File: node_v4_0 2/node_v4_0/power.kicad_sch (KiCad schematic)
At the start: 24 parts, among them J1 Conn_01x02_Pin, J2 12402012E212A, Q1 DMG2301L, U13 MAX31342EWA+T, U3 AP2112K-3.3, U4 CAT3200-5, U5 MCP73831-2-OT

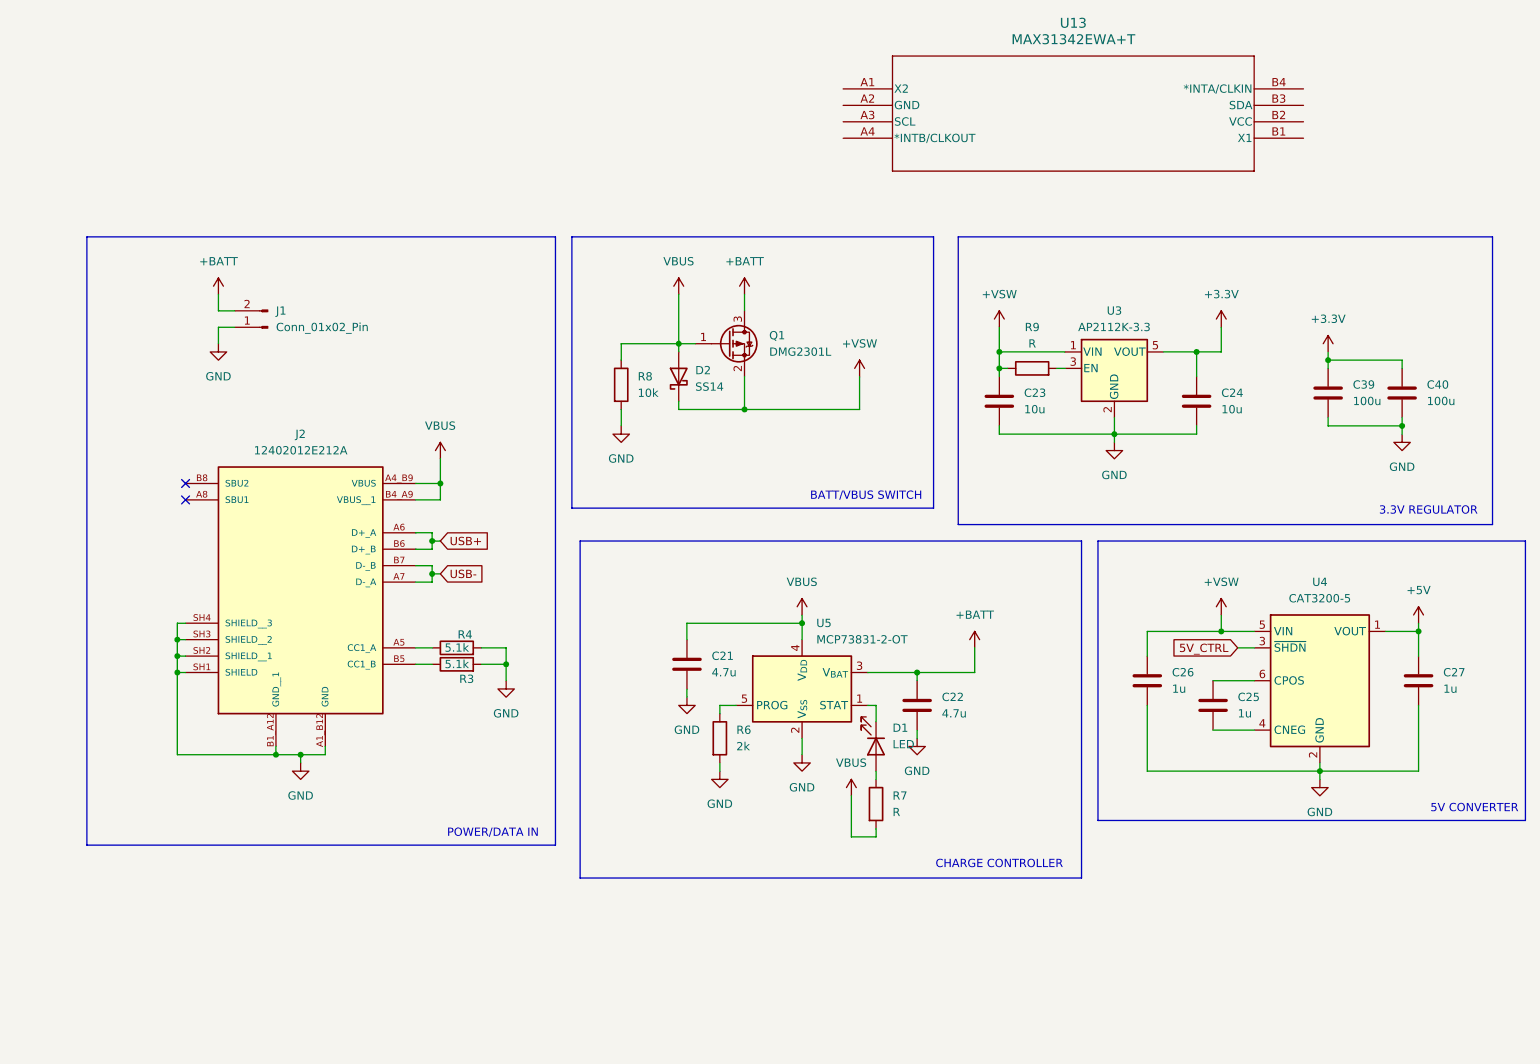
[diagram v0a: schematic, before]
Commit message: finished laying out the board
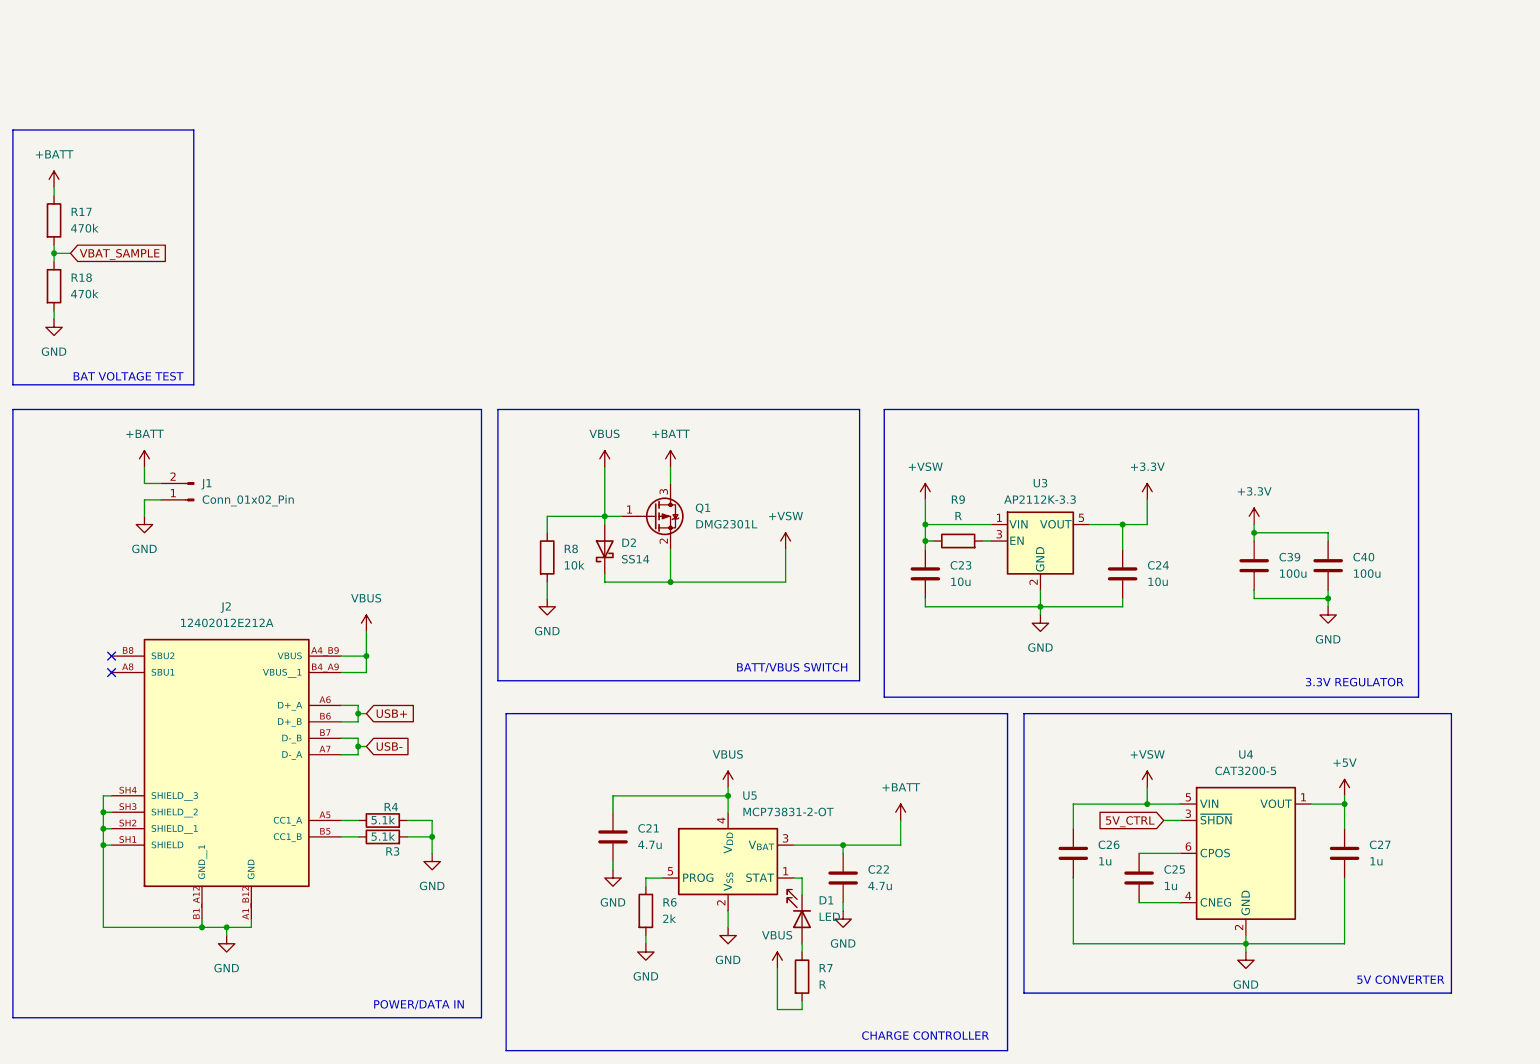
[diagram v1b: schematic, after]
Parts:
- removed U13: MAX31342EWA+T, WiSDOM:21-100291_W80D&plus_1_MXM, symbol WiSDOM:MAX31342EWA+T
- added R17, R18: 470k, Resistor_SMD:R_0805_2012Metric_Pad1.20x1.40mm_HandSolder, symbol Device:R
- J2: footprint usbc:AMPHENOL_12402012E212A -> WiSDOM:AMPHENOL_12402012E212A
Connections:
- net +BATT: now also R17.1
- net GND: now also R18.2
- new net VBAT_SAMPLE: R17.2, R18.1
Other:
- note added: "BAT VOLTAGE TEST"
- moved on the sheet: C21, C22, C23, C24, C25, C26, C27, C39, C40, D1, D2, J1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

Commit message: most routing done
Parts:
- added BT1: RTC_BAT, WiSDOM:BAT_BAT-HLD-001-THM, symbol Device:Battery_Cell
- added C46: 10u, Capacitor_SMD:C_0805_2012Metric_Pad1.18x1.45mm_HandSolder, symbol Device:C
- added D3: SS14, Diode_SMD:D_SMA, symbol Diode:SS14
- added Q2: DMG2301L, Package_TO_SOT_SMD:SOT-23, symbol Transistor_FET:DMG2301L
- added R19: 100k, Resistor_SMD:R_0805_2012Metric_Pad1.20x1.40mm_HandSolder, symbol Device:R
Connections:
- net +3.3V: now also D3.2 (A), Q2.1 (G), R19.1
- net GND: now also BT1.2 (-), C46.2, R19.2
- new net +VRTC: C46.1, D3.1 (K), Q2.2 (S)
- new net RTC_BAT: BT1.1 (+), Q2.3 (D)

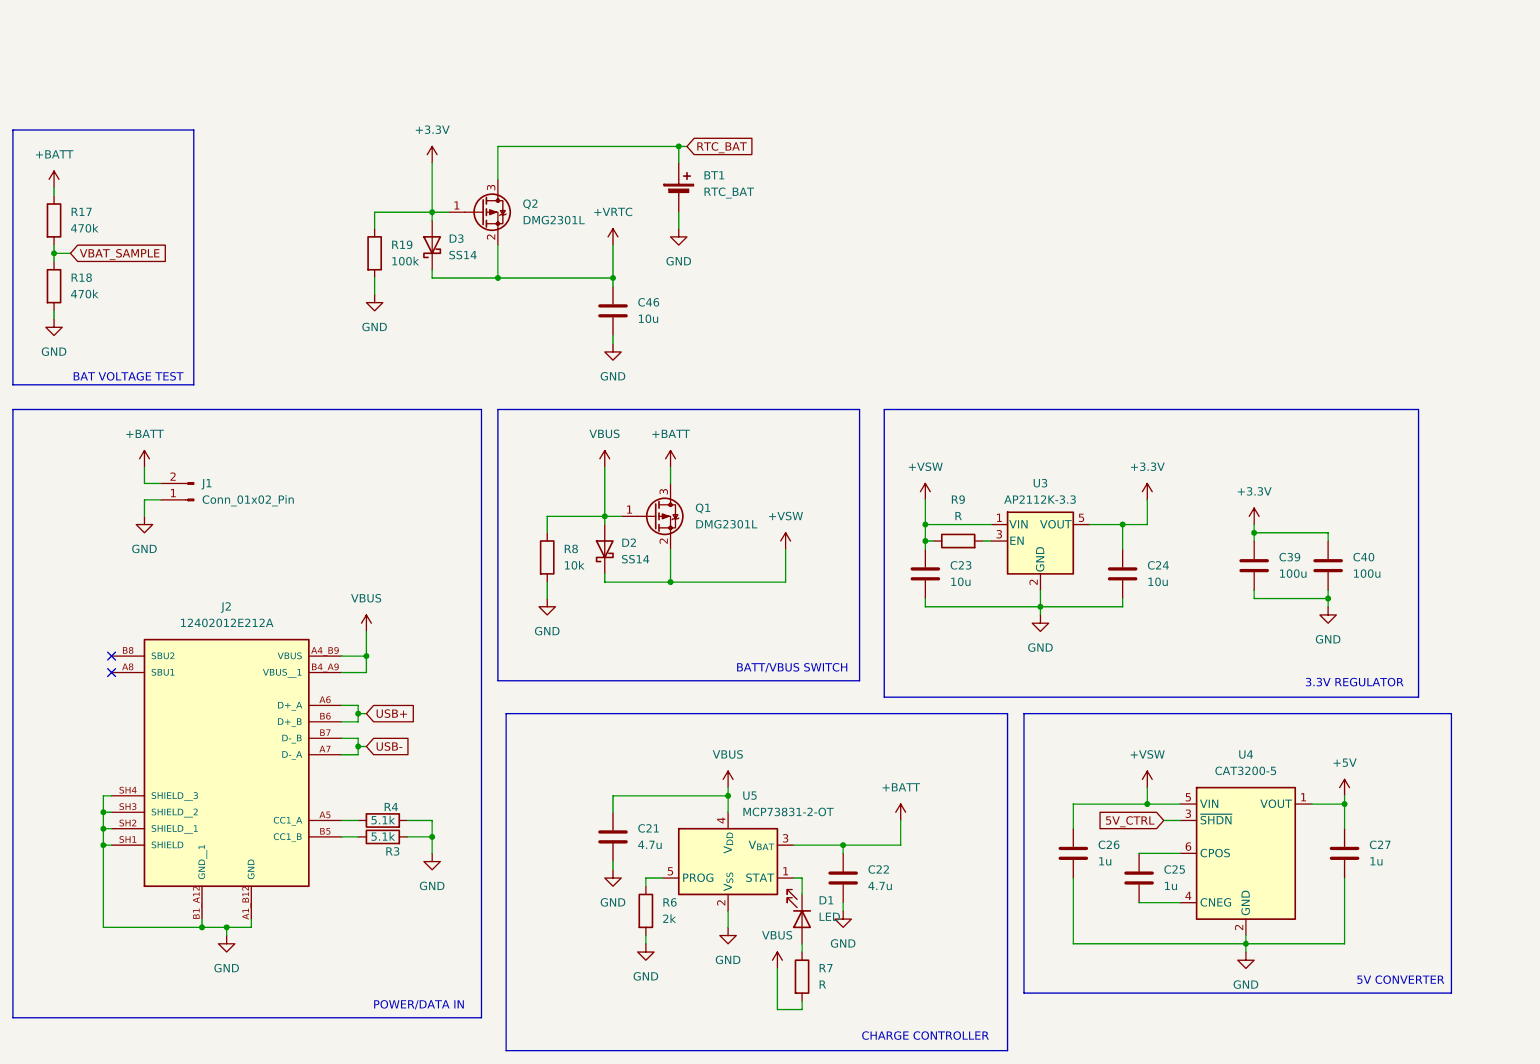
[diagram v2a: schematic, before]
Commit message: moved reset button to make space for vin jst connector
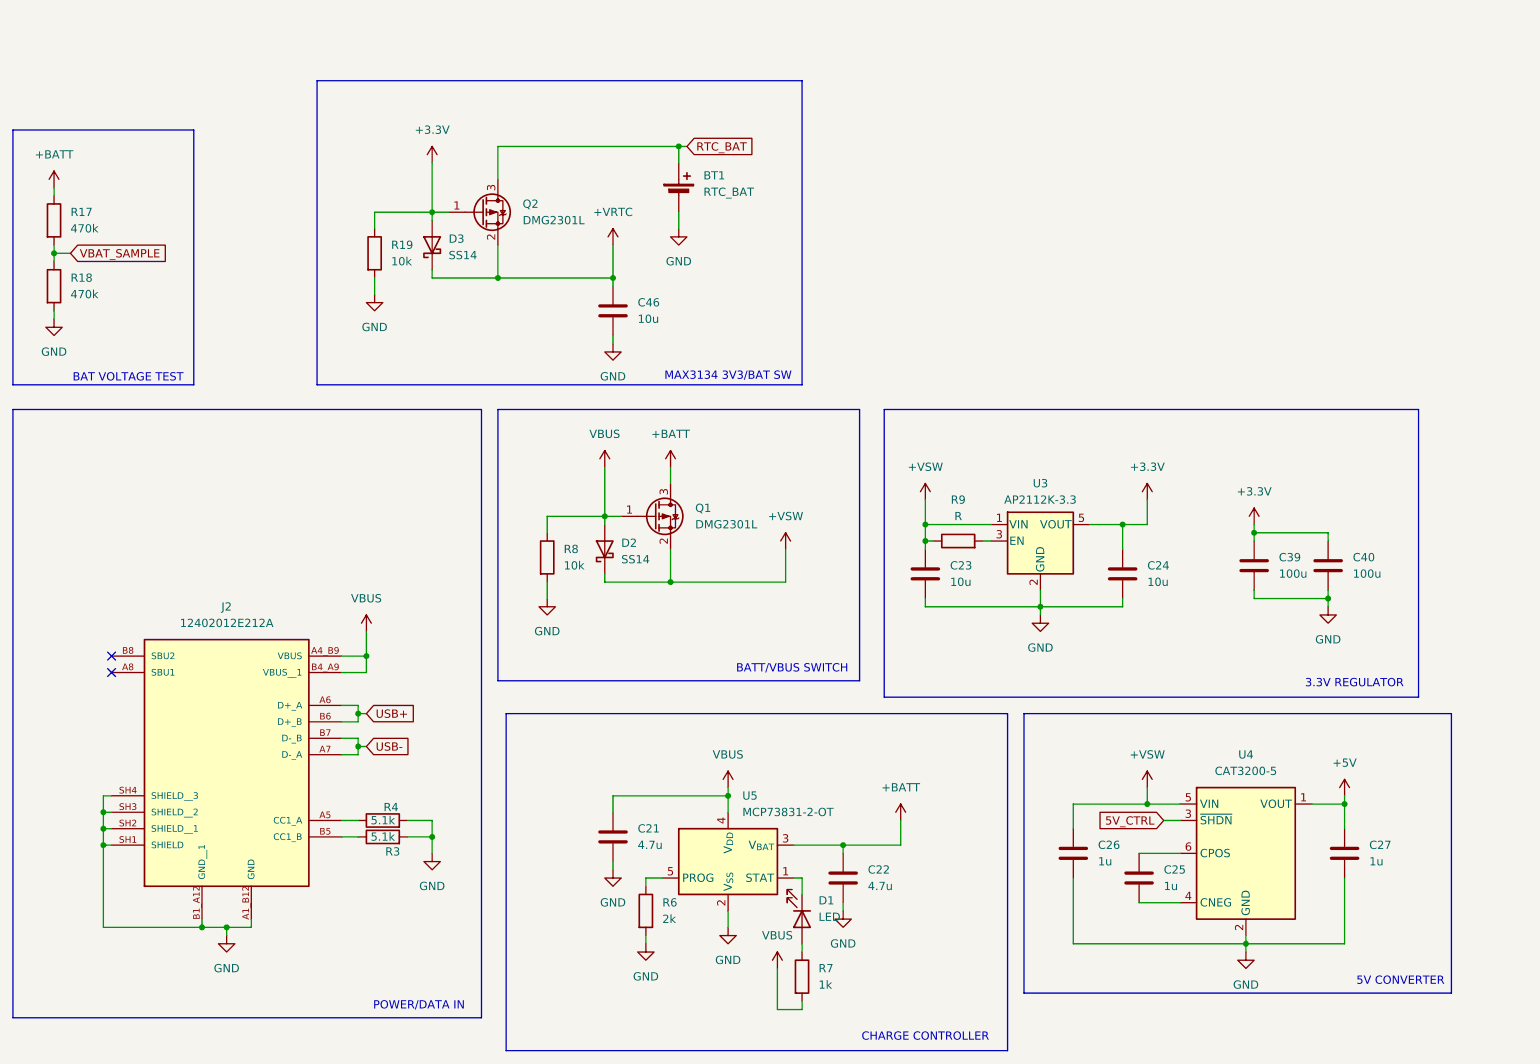
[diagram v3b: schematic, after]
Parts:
- removed J1: Conn_01x02_Pin, Connector_JST:JST_PH_S2B-PH-K_1x02_P2.00mm_Horizontal, symbol Connector:Conn_01x02_Pin
- R19: value 100k -> 10k
- R7: value R -> 1k
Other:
- note added: "MAX3134 3V3/BAT SW"
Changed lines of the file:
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@@
 	(wire
 		(pts
-			(xy 41.91 82.55) (xy 41.91 85.09)
-		)
-		(stroke
-			(width 0)
-			(type default)
-		)
-	)
-	(wire
-		(pts
 			(xy 143.51 166.37) (xy 143.51 165.1)
 		)
@@
 	(wire
 		(pts
-			(xy 41.91 85.09) (xy 44.45 85.09)
-		)
-		(stroke
-			(width 0)
-			(type default)
-		)
-	)
-	(wire
-		(pts
 			(xy 74.93 124.46) (xy 74.93 125.73)
 		)
@@
 	(wire
 		(pts
-			(xy 41.91 87.63) (xy 44.45 87.63)
-		)
-		(stroke
-			(width 0)
-			(type default)
-		)
-	)
-	(wire
-		(pts
 			(xy 124.46 33.02) (xy 96.52 33.02)
 		)
@@
 	(wire
 		(pts
-			(xy 41.91 90.17) (xy 41.91 87.63)
-		)
-		(stroke
-			(width 0)
-			(type default)
-		)
-	)
-	(wire
-		(pts
 			(xy 86.36 43.18) (xy 88.9 43.18)
 		)
@@
 	)
 	(rectangle
+		(start 68.58 22.86)
+		(end 143.51 69.85)
+		(stroke
+			(width 0)
+			(type default)
+		)
+		(fill
+			(type none)
+		)
+	)
+	(rectangle
 		(start 156.21 73.66)
 		(end 238.76 118.11)
@@
 		)
 	)
+	(text "MAX3134 3V3/BAT SW"
+		(exclude_from_sim no)
+		(at 132.08 68.58 0)
+		(effects
+			(font
+				(size 1.27 1.27)
+			)
+		)
+	)
 	(text "BAT VOLTAGE TEST"
 		(exclude_from_sim no)
@@
 			)
 		)
-		(property "Value" "100k"
+		(property "Value" "10k"
 			(at 80.01 50.7999 0)
 			(effects
@@
 	(symbol
 		(lib_id "power:GND")
-		(at 41.91 90.17 0)
-		(unit 1)
-		(exclude_from_sim no)
-		(in_bom yes)
-		(on_board yes)
-		(dnp no)
-		(fields_autoplaced yes)
-		(property "Reference" "#PWR041"
-			(at 41.91 96.52 0)
-			(effects
-				(font
-					(size 1.27 1.27)
-				)
-				(hide yes)
-			)
-		)
-		(property "Value" "GND"
-			(at 41.91 95.25 0)
-			(effects
-				(font
-					(size 1.27 1.27)
-				)
-			)
-		)
-		(property "Footprint" ""
-			(at 41.91 90.17 0)
-			(effects
-				(font
-					(size 1.27 1.27)
-				)
-				(hide yes)
-			)
-		)
-		(property "Datasheet" ""
-			(at 41.91 90.17 0)
-			(effects
-				(font
-					(size 1.27 1.27)
-				)
-				(hide yes)
-			)
-		)
-		(property "Description" "Power symbol creates a global label with name \"GND\" , ground"
-			(at 41.91 90.17 0)
-			(effects
-				(font
-					(size 1.27 1.27)
-				)
-				(hide yes)
-			)
-		)
-		(pin "1"
-		)
-		(instances
-			(project "node_v4_0"
-				(path "/03dc898e-8f05-4377-b5c6-8a0f09836da8/0531f7fa-ef0f-48d8-998a-4014f07ea2d0"
-					(reference "#PWR041")
-					(unit 1)
-				)
-			)
-		)
-	)
-	(symbol
-		(lib_id "power:GND")
 		(at 149.86 151.13 0)
 		(unit 1)
@@
 	)
 	(symbol
-		(lib_id "Connector:Conn_01x02_Pin")
-		(at 49.53 87.63 180)
-		(unit 1)
-		(exclude_from_sim no)
-		(in_bom yes)
-		(on_board yes)
-		(dnp no)
-		(fields_autoplaced yes)
-		(property "Reference" "J1"
-			(at 50.8 85.0899 0)
-			(effects
-				(font
-					(size 1.27 1.27)
-				)
-				(justify right)
-			)
-		)
-		(property "Value" "Conn_01x02_Pin"
-			(at 50.8 87.6299 0)
-			(effects
-				(font
-					(size 1.27 1.27)
-				)
-				(justify right)
-			)
-		)
-		(property "Footprint" "Connector_JST:JST_PH_S2B-PH-K_1x02_P2.00mm_Horizontal"
-			(at 49.53 87.63 0)
-			(effects
-				(font
-					(size 1.27 1.27)
-				)
-				(hide yes)
-			)
-		)
-		(property "Datasheet" "~"
-			(at 49.53 87.63 0)
-			(effects
-				(font
-					(size 1.27 1.27)
-				)
-				(hide yes)
-			)
-		)
-		(property "Description" "Generic connector, single row, 01x02, script generated"
-			(at 49.53 87.63 0)
-			(effects
-				(font
-					(size 1.27 1.27)
-				)
-				(hide yes)
-			)
-		)
-		(pin "2"
-		)
-		(pin "1"
-		)
-		(instances
-			(project ""
-				(path "/03dc898e-8f05-4377-b5c6-8a0f09836da8/0531f7fa-ef0f-48d8-998a-4014f07ea2d0"
-					(reference "J1")
-					(unit 1)
-				)
-			)
-		)
-	)
-	(symbol
 		(lib_id "Device:R")
 		(at 78.74 137.16 90)
@@
 	(symbol
 		(lib_id "power:+BATT")
-		(at 41.91 82.55 0)
-		(unit 1)
-		(exclude_from_sim no)
-		(in_bom yes)
-		(on_board yes)
-		(dnp no)
-		(fields_autoplaced yes)
-		(property "Reference" "#PWR042"
-			(at 41.91 86.36 0)
-			(effects
-				(font
-					(size 1.27 1.27)
-				)
-				(hide yes)
-			)
-		)
-		(property "Value" "+BATT"
-			(at 41.91 77.47 0)
-			(effects
-				(font
-					(size 1.27 1.27)
-				)
-			)
-		)
-		(property "Footprint" ""
-			(at 41.91 82.55 0)
-			(effects
-				(font
-					(size 1.27 1.27)
-				)
-				(hide yes)
-			)
-		)
-		(property "Datasheet" ""
-			(at 41.91 82.55 0)
-			(effects
-				(font
-					(size 1.27 1.27)
-				)
-				(hide yes)
-			)
-		)
-		(property "Description" "Power symbol creates a global label with name \"+BATT\""
-			(at 41.91 82.55 0)
-			(effects
-				(font
-					(size 1.27 1.27)
-				)
-				(hide yes)
-			)
-		)
-		(pin "1"
-		)
-		(instances
-			(project "node_v4_0"
-				(path "/03dc898e-8f05-4377-b5c6-8a0f09836da8/0531f7fa-ef0f-48d8-998a-4014f07ea2d0"
-					(reference "#PWR042")
-					(unit 1)
-				)
-			)
-		)
-	)
-	(symbol
-		(lib_id "power:+BATT")
 		(at 27.94 39.37 0)
 		(unit 1)
@@
 			)
 		)
-		(property "Value" "R"
+		(property "Value" "1k"
 			(at 146.05 162.5599 0)
 			(effects
